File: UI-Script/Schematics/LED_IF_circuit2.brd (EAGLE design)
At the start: 85 x 10 mm, 24 parts, among them Q2 BC547B, Q3 BC547B, Q4 BC547B, Q5 BC547B

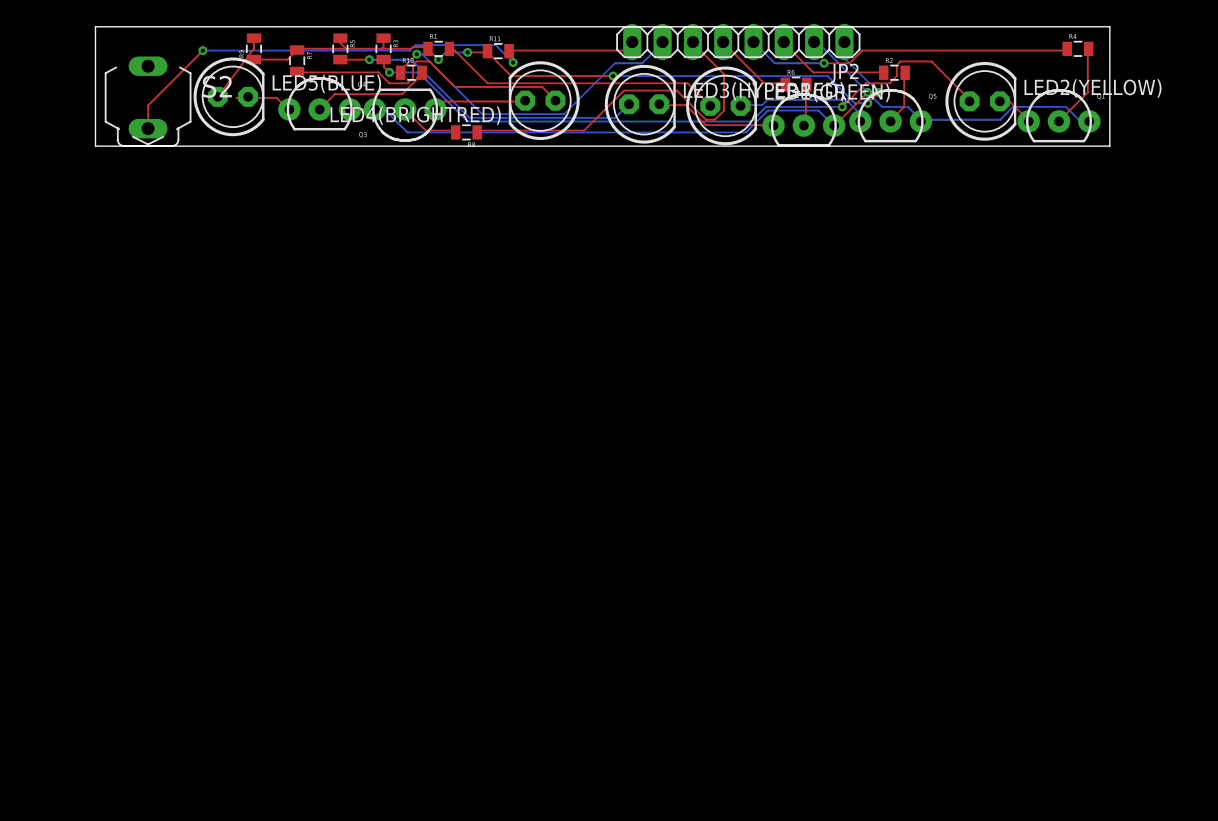
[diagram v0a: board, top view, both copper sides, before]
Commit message: Switched to thru hole
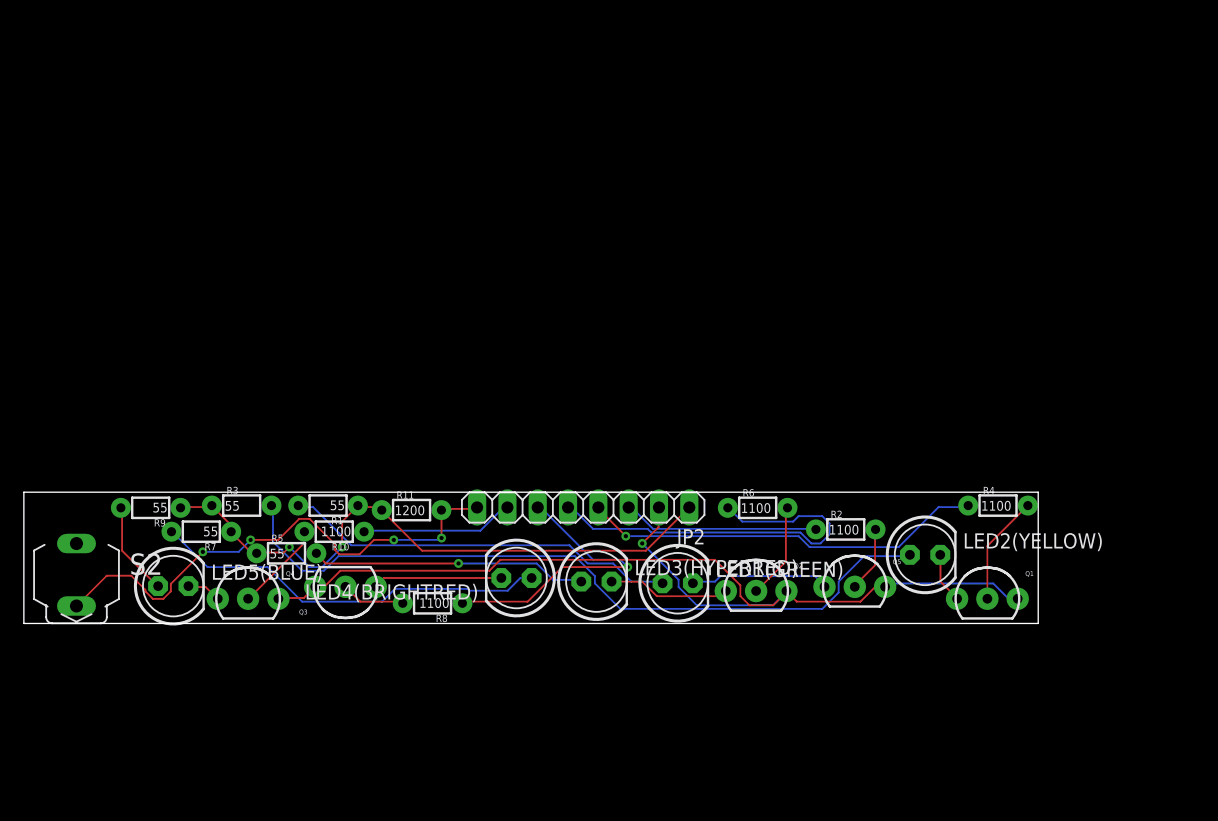
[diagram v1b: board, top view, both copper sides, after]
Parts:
- R1, R10, R11, R2, R3, R4, R5, R6, R7, R8, R9: device SparkFun-Passives:0805 -> SparkFun-Resistors:1/6W-RES
- moved R5 42.5 mm to (22.0, 5.88), turned to 0 degrees
- moved Q4 41.4 mm to (18.8, 2.07)
- moved LED5(BLUE) 41.3 mm to (12.5, 3.13)
- moved JP2 41.1 mm to (46.9, 9.72)
- moved Q1 40.4 mm to (80.7, 2.07)
- moved S2 40.4 mm to (4.41, 5.35)
- moved Q3 40.3 mm to (26.9, 3.07)
- moved R7 40.3 mm to (14.9, 7.69), turned to 180 degrees
- moved LED1(GREEN) 40.2 mm to (54.8, 3.37)
- moved LED3(HYPERRED) 40.2 mm to (48.0, 3.51)
- moved R3 40.1 mm to (18.2, 9.88), turned to 0 degrees
- moved LED4(BRIGHTRED) 40.0 mm to (41.3, 3.81)
- moved R8 39.6 mm to (34.2, 1.69)
- moved R9 39.4 mm to (10.6, 9.69), turned to 180 degrees
- moved R1 39.4 mm to (25.5, 9.88), turned to 180 degrees
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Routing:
- net GPIO3: track 6.70 -> 33.8 mm
- net GPIO5: track 27.4 -> 12.8 mm, vias 1 -> 0
- net GND: track 73.6 -> 86.2 mm
- net VDD: track 63.2 -> 52.2 mm, vias 5 -> 2
- net N$6: track 23.9 -> 33.3 mm
- net N$13: track 24.8 -> 33.5 mm
- net GPIO1: track 9.47 -> 16.5 mm
- net N$9: track 55.7 -> 62.6 mm, vias 2 -> 0
- net GPIO2: track 27.5 -> 33.9 mm
- net GPIO4: track 30.3 -> 24.7 mm, vias 0 -> 1
- net N$14: track 3.55 -> 8.09 mm
- net N$17: track 47.0 -> 43.5 mm, vias 2 -> 4
- net N$15: track 26.7 -> 23.2 mm
- net N$4: track 7.81 -> 10.8 mm
- net N$5: track 5.77 -> 2.89 mm
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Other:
- board size 85 x 10 mm -> 85 x 11 mm

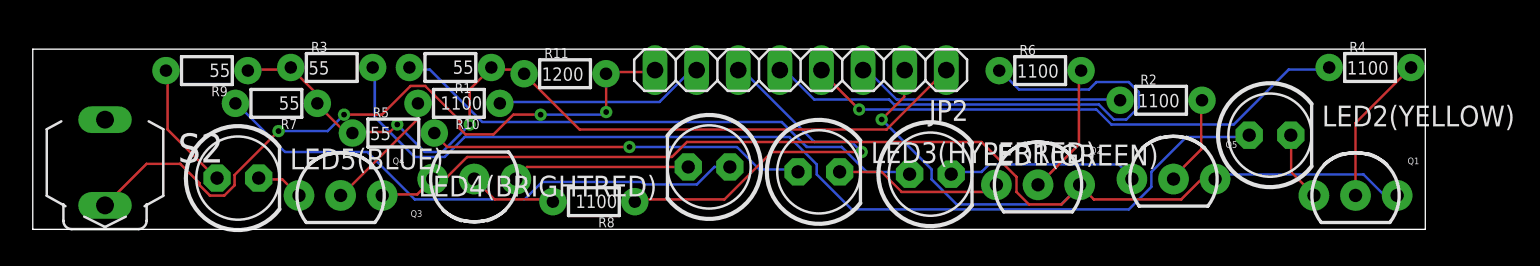
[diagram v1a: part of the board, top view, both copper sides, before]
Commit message: GND copper pours added
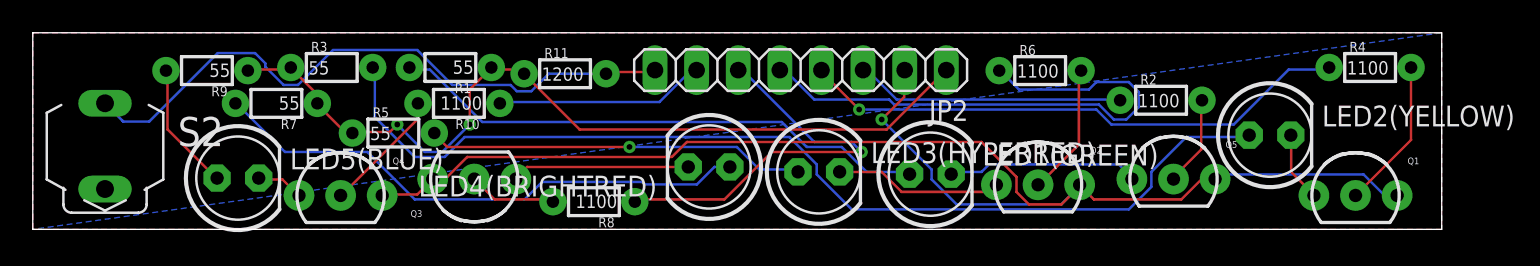
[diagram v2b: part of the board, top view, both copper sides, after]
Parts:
- moved S2 1.00 mm to (4.41, 6.35)
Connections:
- removed net N$7: S2.2
- net GND: now also S2.1
- net N$17: now also S2.2; no longer S2.1
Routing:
- net N$17: track 43.5 -> 39.2 mm, vias 4 -> 0
- added copper zone on layer 1, net GND
- added copper zone on layer 16, net GND
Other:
- board size 85 x 11 mm -> 86 x 12 mm
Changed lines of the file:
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@@
 <board>
 <plain>
-<wire x1="0" y1="0" x2="85" y2="0" width="0" layer="20"/>
-<wire x1="85" y1="0" x2="85" y2="11" width="0" layer="20"/>
-<wire x1="85" y1="11" x2="0" y2="11" width="0" layer="20"/>
-<wire x1="0" y1="11" x2="0" y2="0" width="0" layer="20"/>
+<wire x1="0" y1="0" x2="86" y2="0" width="0" layer="20"/>
+<wire x1="86" y1="0" x2="86" y2="12" width="0" layer="20"/>
+<wire x1="86" y1="12" x2="0" y2="12" width="0" layer="20"/>
+<wire x1="0" y1="12" x2="0" y2="0" width="0" layer="20"/>
 </plain>
 <attributes>
@@
 </class>
 </classes>
-<designrules name="default">
+<designrules name="default *">
 <description language="de">&lt;b&gt;EAGLE Design Rules&lt;/b&gt;
 &lt;p&gt;
@@
 <param name="mdViaViaSameLayer" value="6mil"/>
 <param name="mnLayersViaInSmd" value="2"/>
-<param name="mdCopperDimension" value="40mil"/>
+<param name="mdCopperDimension" value="30mil"/>
 <param name="mdDrill" value="6mil"/>
 <param name="mdSmdStop" value="0mil"/>
@@
 <autorouter>
 <pass name="Default">
-<param name="RoutingGrid" value="50mil"/>
+<param name="RoutingGrid" value="0.25mm"/>
 <param name="AutoGrid" value="1"/>
 <param name="Efforts" value="0"/>
 <param name="TopRouterVariant" value="1"/>
 <param name="tpViaShape" value="round"/>
-<param name="PrefDir.1" value="a"/>
+<param name="PrefDir.1" value="-"/>
 <param name="PrefDir.2" value="0"/>
 <param name="PrefDir.3" value="0"/>
@@
 <param name="PrefDir.14" value="0"/>
 <param name="PrefDir.15" value="0"/>
-<param name="PrefDir.16" value="a"/>
+<param name="PrefDir.16" value="|"/>
 <param name="cfVia" value="8"/>
 <param name="cfNonPref" value="5"/>
@@
 <element name="R8" library="SparkFun-Resistors" package="1/6W-RES" value="1100" x="34.25" y="1.69" rot="R180"/>
 <element name="R9" library="SparkFun-Resistors" package="1/6W-RES" value="55" x="10.63" y="9.69" rot="R180"/>
-<element name="S2" library="switch" package="MS243" value="" x="4.41" y="5.35"/>
+<element name="S2" library="switch" package="MS243" value="" x="4.41" y="6.35"/>
 </elements>
 <signals>
@@
 <contactref element="Q1" pad="2"/>
 <contactref element="R4" pad="2"/>
-<wire x1="84.13" y1="9.88" x2="80.74" y2="6.49" width="0.1524" layer="1"/>
-<wire x1="80.74" y1="6.49" x2="80.74" y2="2.07" width="0.1524" layer="1"/>
+<wire x1="84.13" y1="9.88" x2="84.13" y2="5.46" width="0.1524" layer="1"/>
+<wire x1="84.13" y1="5.46" x2="80.74" y2="2.07" width="0.1524" layer="1"/>
 </signal>
 <signal name="GND">
@@
 <wire x1="63.8556" y1="2.5908" x2="63.9" y2="2.72" width="0.1524" layer="1"/>
 <via x="51.816" y="6.7056" extent="1-16" drill="0.35"/>
+<polygon width="0.1524" layer="1" isolate="0.012">
+<vertex x="0" y="0"/>
+<vertex x="0" y="12"/>
+<vertex x="86" y="12"/>
+<vertex x="86" y="0"/>
+</polygon>
+<polygon width="0.1524" layer="16" isolate="0.012">
+<vertex x="0" y="0"/>
+<vertex x="0" y="12"/>
+<vertex x="86" y="12"/>
+</polygon>
+<contactref element="S2" pad="1"/>
 </signal>
 <signal name="N$11">
@@
 <contactref element="JP2" pad="8"/>
 <contactref element="R11" pad="2"/>
-<contactref element="S2" pad="1"/>
 <wire x1="35.052" y1="9.6012" x2="37.9476" y2="9.6012" width="0.1524" layer="1"/>
 <wire x1="37.9476" y1="9.6012" x2="37.98" y2="9.72" width="0.1524" layer="1"/>
 <wire x1="35.052" y1="9.6012" x2="34.99" y2="9.5" width="0.1524" layer="1"/>
-<wire x1="34.99" y1="9.5" x2="35" y2="9.49" width="0.1524" layer="1"/>
-<wire x1="35" y1="9.49" x2="35" y2="7.16" width="0.1524" layer="1"/>
-<wire x1="35" y1="7" x2="35" y2="7.16" width="0.1524" layer="1"/>
-<wire x1="35" y1="7.16" x2="35" y2="7" width="0.1524" layer="1"/>
-<via x="35" y="7.16" extent="1-16" drill="0.35"/>
-<wire x1="35" y1="7.16" x2="34.84" y2="7" width="0.1524" layer="16"/>
-<wire x1="34.84" y1="7" x2="31" y2="7" width="0.1524" layer="16"/>
-<via x="31" y="7" extent="1-16" drill="0.35"/>
-<wire x1="31" y1="7" x2="29.3286875" y2="7" width="0.1524" layer="1"/>
-<wire x1="26.41865" y1="5.794" x2="26.0632" y2="6.14945" width="0.1524" layer="1"/>
-<wire x1="23.9518875" y1="8.7568" x2="23.0681125" y2="8.7568" width="0.1524" layer="1"/>
-<wire x1="26.0632" y1="6.14945" x2="26.0632" y2="6.6454875" width="0.1524" layer="1"/>
-<wire x1="26.0632" y1="6.6454875" x2="23.9518875" y2="8.7568" width="0.1524" layer="1"/>
-<wire x1="21.3113125" y1="7" x2="19" y2="7" width="0.1524" layer="1"/>
-<wire x1="23.0681125" y1="8.7568" x2="21.3113125" y2="7" width="0.1524" layer="1"/>
-<wire x1="29.3286875" y1="7" x2="28.1226875" y2="5.794" width="0.1524" layer="1"/>
-<wire x1="28.1226875" y1="5.794" x2="26.41865" y2="5.794" width="0.1524" layer="1"/>
-<via x="19" y="7" extent="1-16" drill="0.35"/>
-<wire x1="19" y1="7" x2="18" y2="6" width="0.1524" layer="16"/>
-<via x="15" y="6" extent="1-16" drill="0.35"/>
-<wire x1="18" y1="6" x2="15" y2="6" width="0.1524" layer="16"/>
-<wire x1="4.41" y1="1.4638" x2="6.9462" y2="4" width="0.1524" layer="1"/>
-<wire x1="6.9462" y1="4" x2="9" y2="4" width="0.1524" layer="1"/>
-<wire x1="10.1832" y1="2.6881125" x2="10.8081125" y2="2.0632" width="0.1524" layer="1"/>
-<wire x1="10.8081125" y1="2.0632" x2="11.6918875" y2="2.0632" width="0.1524" layer="1"/>
-<wire x1="11.6918875" y1="2.0632" x2="12.3168" y2="2.6881125" width="0.1524" layer="1"/>
-<wire x1="9" y1="4" x2="10.1832" y2="2.8168" width="0.1524" layer="1"/>
-<wire x1="10.1832" y1="2.8168" x2="10.1832" y2="2.6881125" width="0.1524" layer="1"/>
-<wire x1="12.3168" y1="2.6881125" x2="12.3168" y2="3.3168" width="0.1524" layer="1"/>
-<wire x1="12.3168" y1="3.3168" x2="15" y2="6" width="0.1524" layer="1"/>
-</signal>
-<signal name="N$7">
 <contactref element="S2" pad="2"/>
+<wire x1="30.4318875" y1="8.4332" x2="29.5481125" y2="8.4332" width="0.1524" layer="16"/>
+<wire x1="16.1918875" y1="8.8132" x2="15.3081125" y2="8.8132" width="0.1524" layer="16"/>
+<wire x1="14.1968" y1="10.1318875" x2="13.5718875" y2="10.7568" width="0.1524" layer="16"/>
+<wire x1="7.1085625" y1="6.5786" x2="5.5214375" y2="6.5786" width="0.1524" layer="16"/>
+<wire x1="5.5214375" y1="6.5786" x2="5.4768" y2="6.6232375" width="0.1524" layer="16"/>
+<wire x1="34.99" y1="9.5" x2="31.4986875" y2="9.5" width="0.1524" layer="16"/>
+<wire x1="29.5481125" y1="8.4332" x2="29.1681125" y2="8.8132" width="0.1524" layer="16"/>
+<wire x1="14.1968" y1="9.9245125" x2="14.1968" y2="10.1318875" width="0.1524" layer="16"/>
+<wire x1="31.4986875" y1="9.5" x2="30.4318875" y2="8.4332" width="0.1524" layer="16"/>
+<wire x1="15.3081125" y1="8.8132" x2="14.1968" y2="9.9245125" width="0.1524" layer="16"/>
+<wire x1="5.4768" y1="6.6232375" x2="5.4768" y2="6.6294" width="0.1524" layer="16"/>
+<wire x1="5.4768" y1="6.6294" x2="4.41" y2="7.6962" width="0.1524" layer="16"/>
+<wire x1="29.1681125" y1="8.8132" x2="25.60305625" y2="8.8132" width="0.1524" layer="16"/>
+<wire x1="25.60305625" y1="8.8132" x2="23.46945625" y2="10.9468" width="0.1524" layer="16"/>
+<wire x1="18.3254875" y1="10.9468" x2="16.1918875" y2="8.8132" width="0.1524" layer="16"/>
+<wire x1="13.5718875" y1="10.7568" x2="11.2867625" y2="10.7568" width="0.1524" layer="16"/>
+<wire x1="11.2867625" y1="10.7568" x2="7.1085625" y2="6.5786" width="0.1524" layer="16"/>
+<wire x1="23.46945625" y1="10.9468" x2="18.3254875" y2="10.9468" width="0.1524" layer="16"/>
 </signal>
 </signals>
+<errors>
+</errors>
 </board>
 </drawing>

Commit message: PCB update
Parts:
- Q1: value (none) -> MMBT5088; device SparkFun-DiscreteSemi:TO-92-AMMO -> SparkFun-DiscreteSemi:SOT23-3
- Q2, Q3, Q4, Q5: value BC547B -> MMBT5088; device SparkFun-DiscreteSemi:TO-92-AMMO -> SparkFun-DiscreteSemi:SOT23-3
- R1, R3, R5, R7, R9: value 55 -> 1100; device SparkFun-Resistors:1/6W-RES -> SparkFun-Passives:0603-RES
- R10, R2, R4, R6, R8: value 1100 -> 55; device SparkFun-Resistors:1/6W-RES -> SparkFun-Passives:0603-RES
- R11: device SparkFun-Resistors:1/6W-RES -> SparkFun-Passives:0603-RES
- moved R10 53.2 mm to (79.2, 8.27), turned to 90 degrees
- moved R8 43.5 mm to (77.6, 5.06)
- moved R9 27.9 mm to (38.5, 7.65), turned to 90 degrees
- moved R7 27.2 mm to (42.0, 7.62), turned to 90 degrees
- moved Q1 25.2 mm to (56.4, 8.56), turned to 270 degrees
- moved LED3(HYPERRED) 25.2 mm to (73.2, 3.17), turned to 90 degrees
- moved R5 24.9 mm to (46.5, 1.88), turned to 90 degrees
- moved R2 19.9 mm to (49.8, 1.94), turned to 270 degrees
- moved R6 17.7 mm to (77.4, 1.96), turned to 90 degrees
- moved R11 16.4 mm to (48.8, 7.75), turned to 90 degrees
- moved R3 16.2 mm to (34.4, 8.19), turned to 180 degrees
- moved R4 16.2 mm to (67.7, 1.59), turned to 180 degrees
- moved JP2 14.8 mm to (33.7, 2.90)
- moved LED2(YELLOW) 13.9 mm to (61.9, 3.04), turned to 270 degrees
- moved Q2 13.7 mm to (74.0, 7.87), turned to 270 degrees
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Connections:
- removed net GPIO3: JP2.5, R6.1
- new net N$18: JP2.5, R5.1
- net GND: now also Q1.2, Q2.2, Q3.2, Q4.2, Q5.2; no longer Q1.3, Q2.3, Q3.3, Q4.3, Q5.3
- net GPIO1: now also R9.1; no longer R2.1
- net GPIO2: now also R7.1; no longer R4.1
- net GPIO4: now also R3.1; no longer R8.1
- net GPIO5: now also R1.1; no longer R10.1
- net N$1: now also Q5.3; no longer Q5.1
- net N$10: now also Q1.1, R7.2; no longer Q1.2, R4.2
- net N$11: now also R2.2; no longer R9.2
- net N$12: now also Q3.1, R3.2; no longer Q3.2, R8.2
- net N$13: now also R4.2; no longer R7.2
- net N$14: now also Q2.1, R5.2; no longer Q2.2, R6.2
- net N$15: now also R6.2; no longer R5.2
- net N$16: now also Q4.1, R1.2; no longer Q4.2, R10.2
- net N$2: now also Q1.3; no longer Q1.1
- net N$3: now also Q2.3; no longer Q2.1
- net N$4: now also Q3.3; no longer Q3.1
- net N$5: now also Q4.3; no longer Q4.1
- net N$6: now also R10.2; no longer R1.2
- net N$8: now also Q5.1, R9.2; no longer Q5.2, R2.2
- net N$9: now also R8.2; no longer R3.2
- net VDD: now also R10.1, R2.1, R4.1, R6.1, R8.1; no longer R1.1, R3.1, R5.1, R7.1, R9.1
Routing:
- net N$9: track 62.6 -> 16.0 mm
- net GPIO3: track 33.8 -> 0.00 mm
- net N$11: track 7.88 -> 41.0 mm, vias 0 -> 2
- net GPIO2: track 33.9 -> 9.53 mm, vias 1 -> 2
- net N$14: track 8.09 -> 30.1 mm, vias 0 -> 2
- net N$13: track 33.5 -> 13.3 mm, vias 0 -> 1
- net GND: track 86.2 -> 66.8 mm, vias 1 -> 5
- net N$6: track 33.3 -> 14.2 mm, vias 0 -> 1
- net N$15: track 23.2 -> 4.57 mm, vias 1 -> 0
- net N$8: track 5.52 -> 23.7 mm, vias 0 -> 2
- net GPIO4: track 24.7 -> 7.59 mm, vias 1 -> 0
- net VDD: track 52.2 -> 69.3 mm, vias 2 -> 1
- net N$18: track 0.00 -> 16.6 mm
- net N$4: track 10.8 -> 26.4 mm, vias 0 -> 1
- net GPIO1: track 16.5 -> 4.31 mm
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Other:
- board size 86 x 12 mm -> 84 x 11.1 mm

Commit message: no error DRC
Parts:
- moved R2 1.20 mm to (49.5, 3.08)
- moved R5 1.15 mm to (46.4, 3.02)
- moved R6 0.57 mm to (77.6, 2.47)
- moved Q5 0.51 mm to (61.8, 8.73)
- moved LED2(YELLOW) 0.28 mm to (61.8, 3.30)
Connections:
- net N$18 renamed GPIO3
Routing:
- net N$2: track 8.85 -> 11.2 mm
- net GPIO3: track 16.6 -> 15.5 mm
- net N$8: track 23.7 -> 24.7 mm
- net VDD: track 69.3 -> 68.6 mm
- net N$14: track 30.1 -> 29.4 mm
- net N$15: track 4.57 -> 5.12 mm
- net GND: track 66.8 -> 67.4 mm
